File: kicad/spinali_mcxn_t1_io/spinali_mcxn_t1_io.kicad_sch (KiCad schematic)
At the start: 0 parts

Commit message: Added Rev-A in MR-MCXN-T1-IO
- Added Rev-A in schematic and layout
- Created production files

Signed-off-by: Youri Tils <youri.tils@nxp.com>
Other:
- company: NXP SEMICONDUCTORS B.V. -> ${COMPANY}
- title: MR-MCXN-T1-IO -> ${TITLE}
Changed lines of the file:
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@@
 	(paper "A4")
 	(title_block
-		(title "MR-MCXN-T1-IO")
-		(date "2026-07-24")
-		(rev "X1")
-		(company "NXP SEMICONDUCTORS B.V.")
-		(comment 1 "DESIGNER: YOURI TILS")
-		(comment 2 "CTO SYSTEM INNOVATIONS / MOBILE ROBOTICS DOMAIN")
+		(title "${TITLE}")
+		(date "2026-08-24")
+		(rev "${BOARD_REV}")
+		(company "${COMPANY}")
+		(comment 1 "DESIGNER: ${DESIGNER}")
+		(comment 2 "${DEPARTMENT}")
+		(comment 3 "REVIEWED BY: ${REVIEWER}")
 	)
 	(text "MR-MCXN-T1 IO"

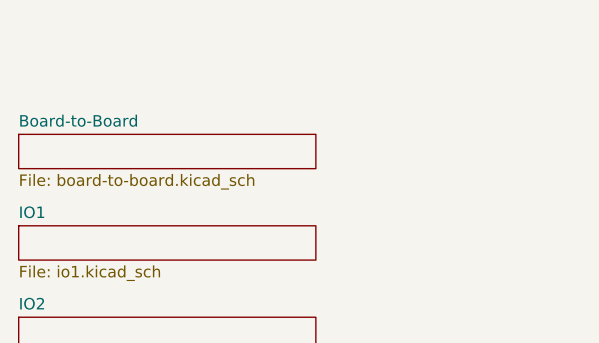
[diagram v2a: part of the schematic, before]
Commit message: BD update on F9P and IO
Updates to block diagrams for -F9P and -IO shields.
No schematic functionality change.
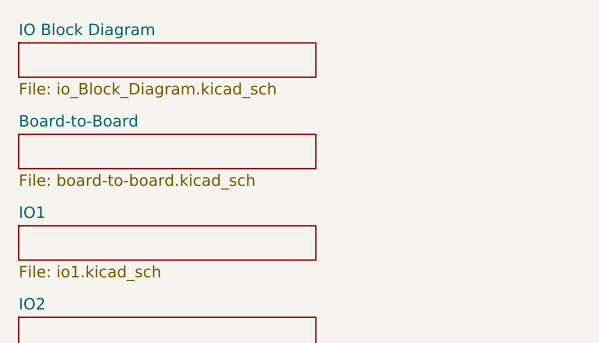
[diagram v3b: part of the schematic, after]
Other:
- added sheet IO Block Diagram (io_Block_Diagram.kicad_sch)
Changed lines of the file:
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@@
+	)
+	(sheet
+		(at 29.21 36.83)
+		(size 33.02 3.81)
+		(exclude_from_sim no)
+		(in_bom yes)
+		(on_board yes)
+		(dnp no)
+		(fields_autoplaced yes)
+		(stroke
+			(width 0.1524)
+			(type solid)
+		)
+		(fill
+			(color 0 0 0 0.0000)
+		)
+		(property "Sheetname" "IO Block Diagram"
+			(at 29.21 36.1184 0)
+			(effects
+				(font
+					(size 1.27 1.27)
+				)
+				(justify left bottom)
+			)
+		)
+		(property "Sheetfile" "io_Block_Diagram.kicad_sch"
+			(at 29.21 41.2246 0)
+			(effects
+				(font
+					(size 1.27 1.27)
+				)
+				(justify left top)
+			)
+		)
+		(instances
+			(project "spinali_mcxn_t1_io"
+				(path "/04285d74-eeba-483c-9378-52bd287e15a2"
+					(page "5")
+				)
+			)
+		)
 	)
 	(sheet
